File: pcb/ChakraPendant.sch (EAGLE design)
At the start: 12 parts

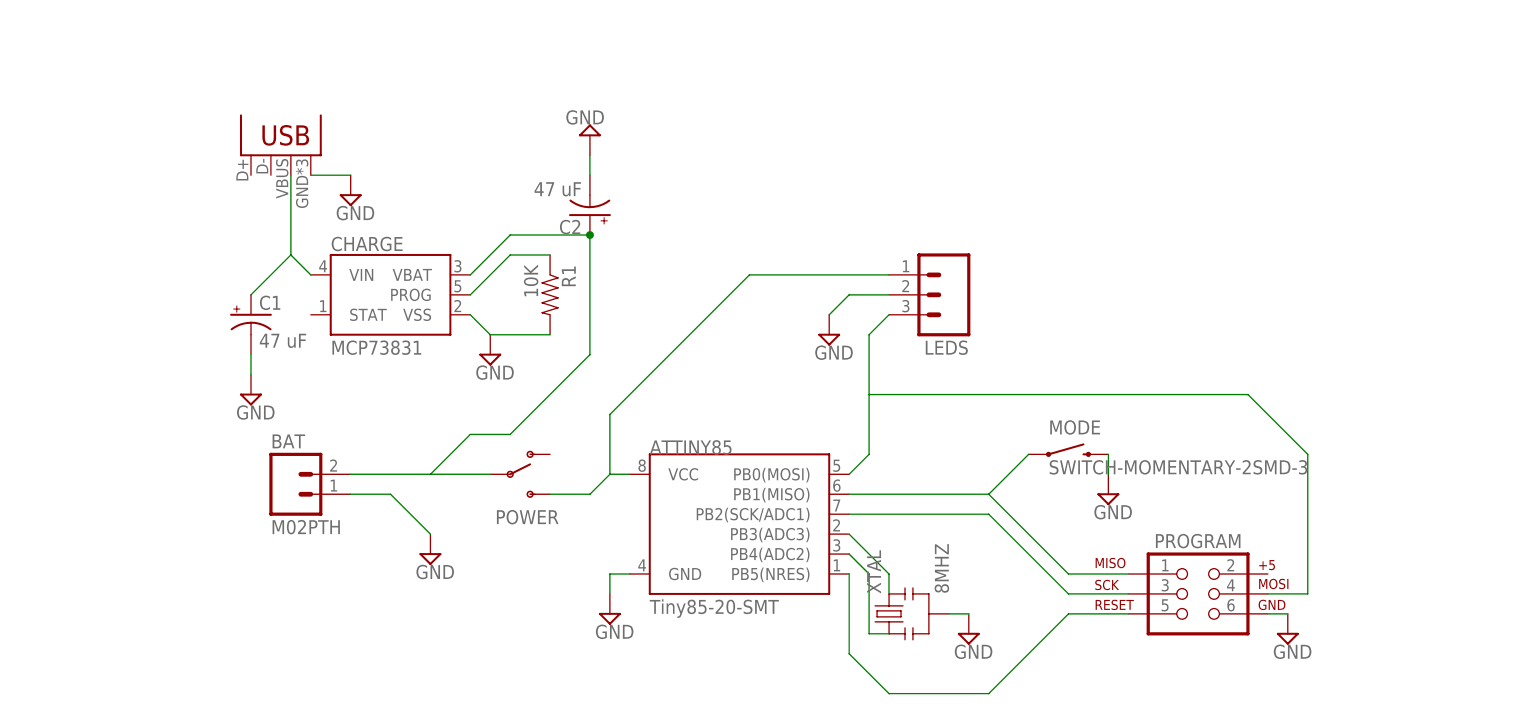
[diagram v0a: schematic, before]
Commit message: Remove power switches. Add Charge LEDs. Change ISP header to pogopin programmer.
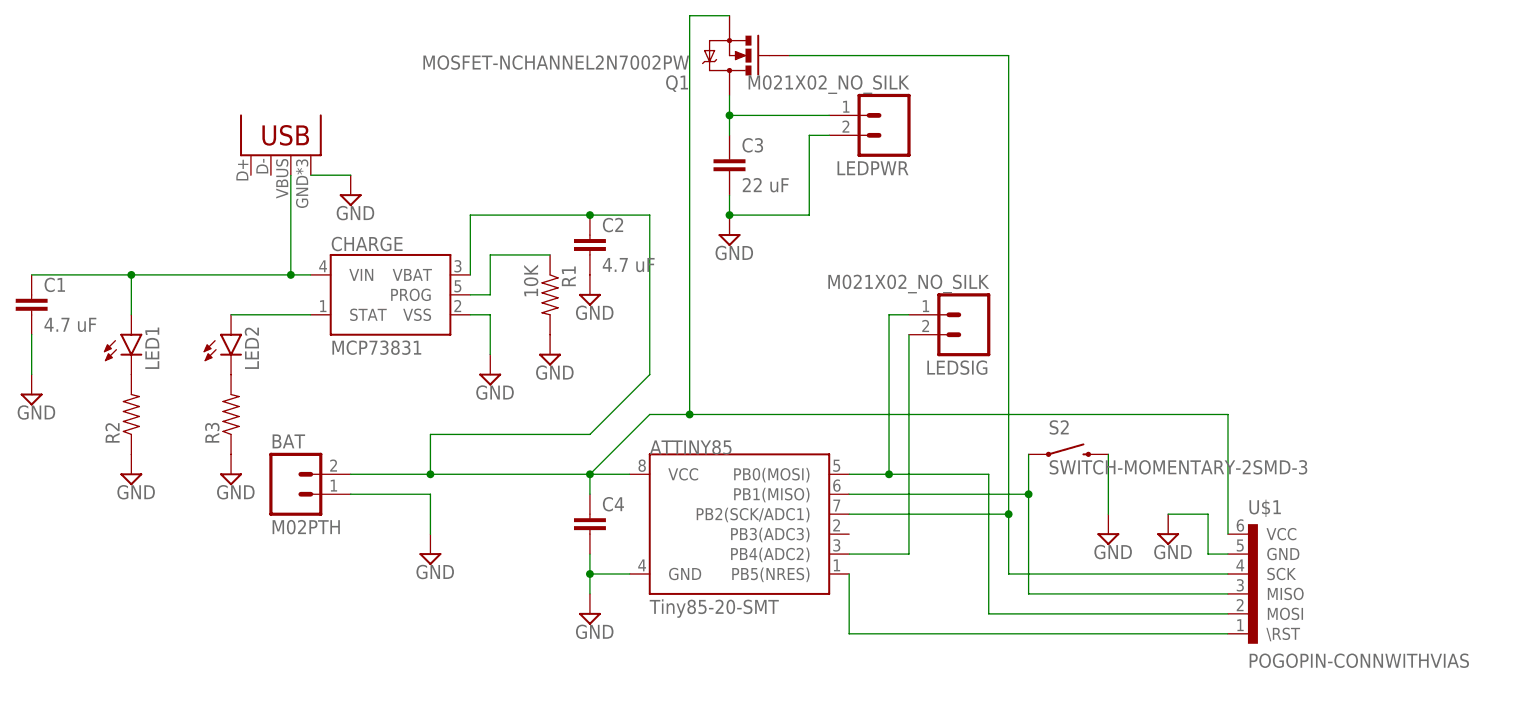
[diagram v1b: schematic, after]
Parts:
- removed LEDS: (no value), SparkFun-Connectors:M03PTH
- removed POWER: (no value), SparkFun-Electromechanical:SWITCH-SPDT-SMD-A
- removed PROGRAM: AVR_SPI_PRG_62X3_LOCK, SparkFun-Connectors:AVR_SPI_PRG_62X3_LOCK
- removed XTAL: 8MHZ, SparkFun-FreqCtrl:RESONATOR8MHZ
- added C3: 22 uF, SparkFun-Passives:CAP1206
- added C4: (no value), SparkFun-Passives:CAP0603-CAP
- added LED1, LED2: (no value), SparkFun-LED:LED0603
- added LEDPWR, LEDSIG: M021X02_NO_SILK, SparkFun-Connectors:M021X02_NO_SILK
- added Q1: MOSFET-NCHANNEL2N7002PW, SparkFun-DiscreteSemi:MOSFET-NCHANNEL2N7002PW
- added R2, R3: (no value), SparkFun-Passives:RESISTOR0603-RES
- added U$1: POGOPIN-CONNWITHVIAS, Protofusion:POGOPIN-CONNWITHVIAS
- C1, C2: value 47 uF -> 4.7 uF; device SparkFun-Capacitors:CAP_POL1206 -> SparkFun-Passives:CAP0603-CAP
- renumbered MODE to S2
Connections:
- removed net USBV+: C1.+, CHARGE.VIN, JP1.VBUS
- removed net VCC: ATTINY85.VCC, LEDS.1, POWER.S
- removed net XTAL1: ATTINY85.PB4(ADC2), XTAL.1
- removed net XTAL2: ATTINY85.PB3(ADC3), XTAL.3
- new net N$1: C3.1, LEDPWR.1, Q1.D
- new net N$2: C1.1, CHARGE.VIN, JP1.VBUS, LED1.A
- new net N$3: ATTINY85.PB4(ADC2), LEDSIG.2
- new net N$4: LED1.C, R2.2
- new net N$5: LED2.C, R3.2
- new net N$7: CHARGE.STAT, LED2.A
- net BATTV+: now also ATTINY85.VCC, C2.1, C4.1, Q1.S, U$1.VCC; no longer C2.+, POWER.P
- net GND: now also C1.2, C2.2, C3.2, C4.2, LEDPWR.2, R2.1, R3.1, U$1.GND; no longer C1.-, C2.-, LEDS.2, PROGRAM.6, XTAL.2
- net PB0-MOSI: now also LEDSIG.1, U$1.MOSI; no longer LEDS.3, PROGRAM.4
- net PB1-MISO: now also U$1.MISO; no longer PROGRAM.1
- net PB2-SCK: now also Q1.G, U$1.SCK; no longer PROGRAM.3
- net PB5-RESET: now also U$1.\RST; no longer PROGRAM.5

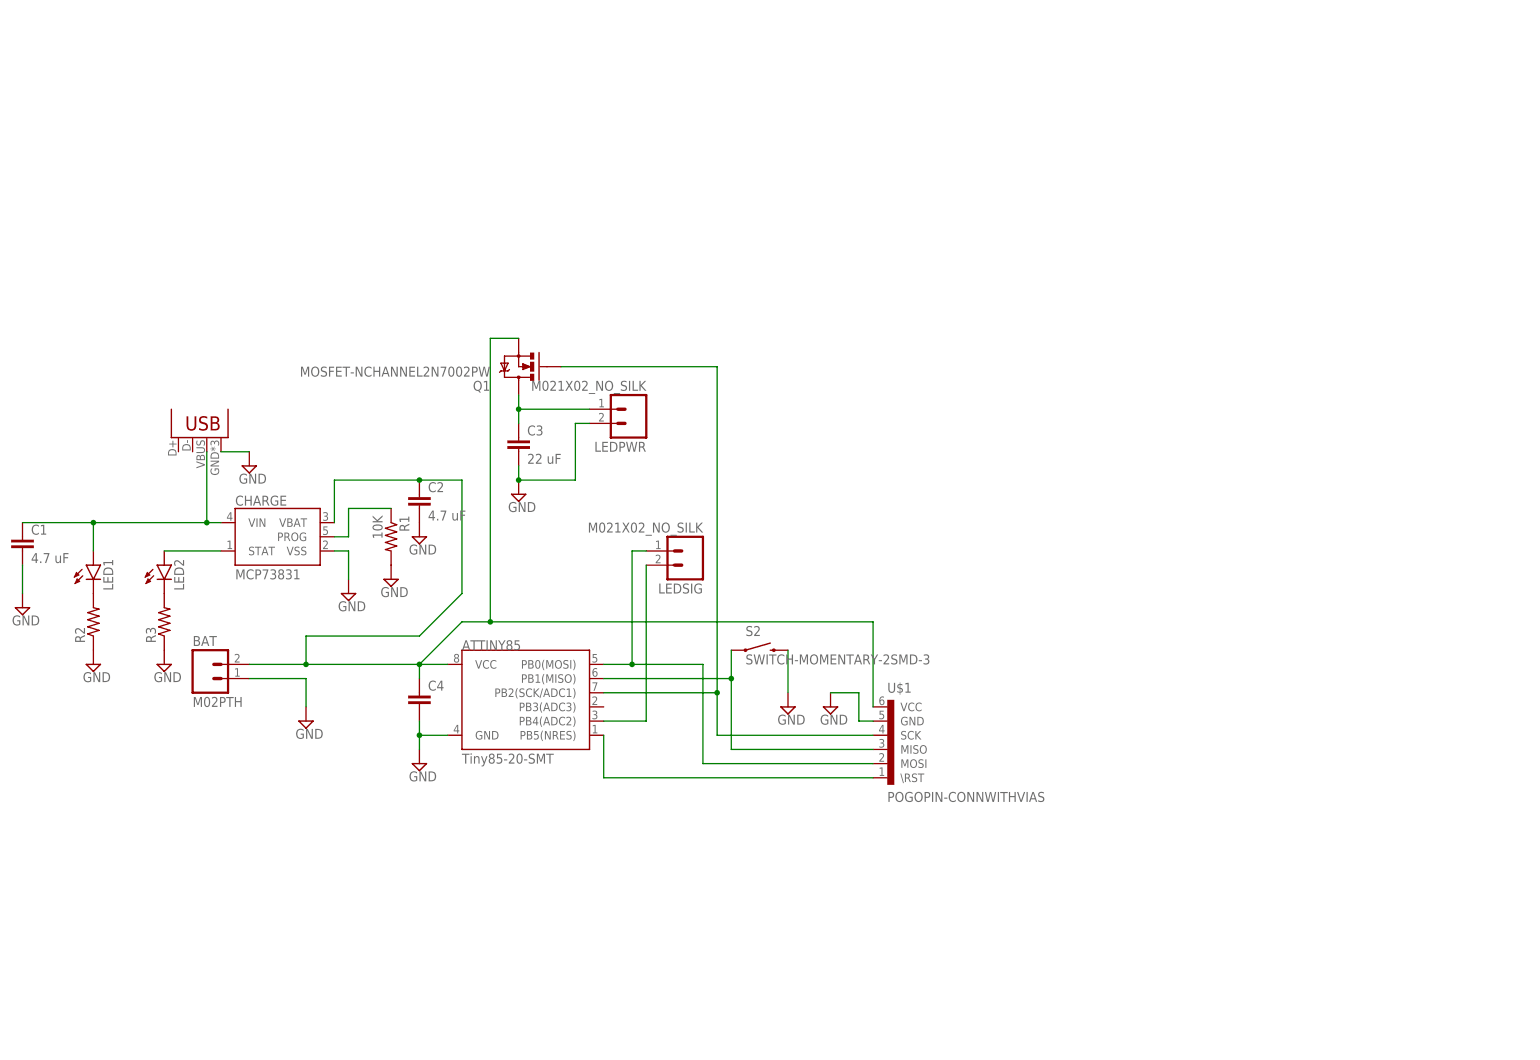
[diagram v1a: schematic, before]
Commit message: GREATLY cleaned up main board schematic. Piped charge STAT to chip
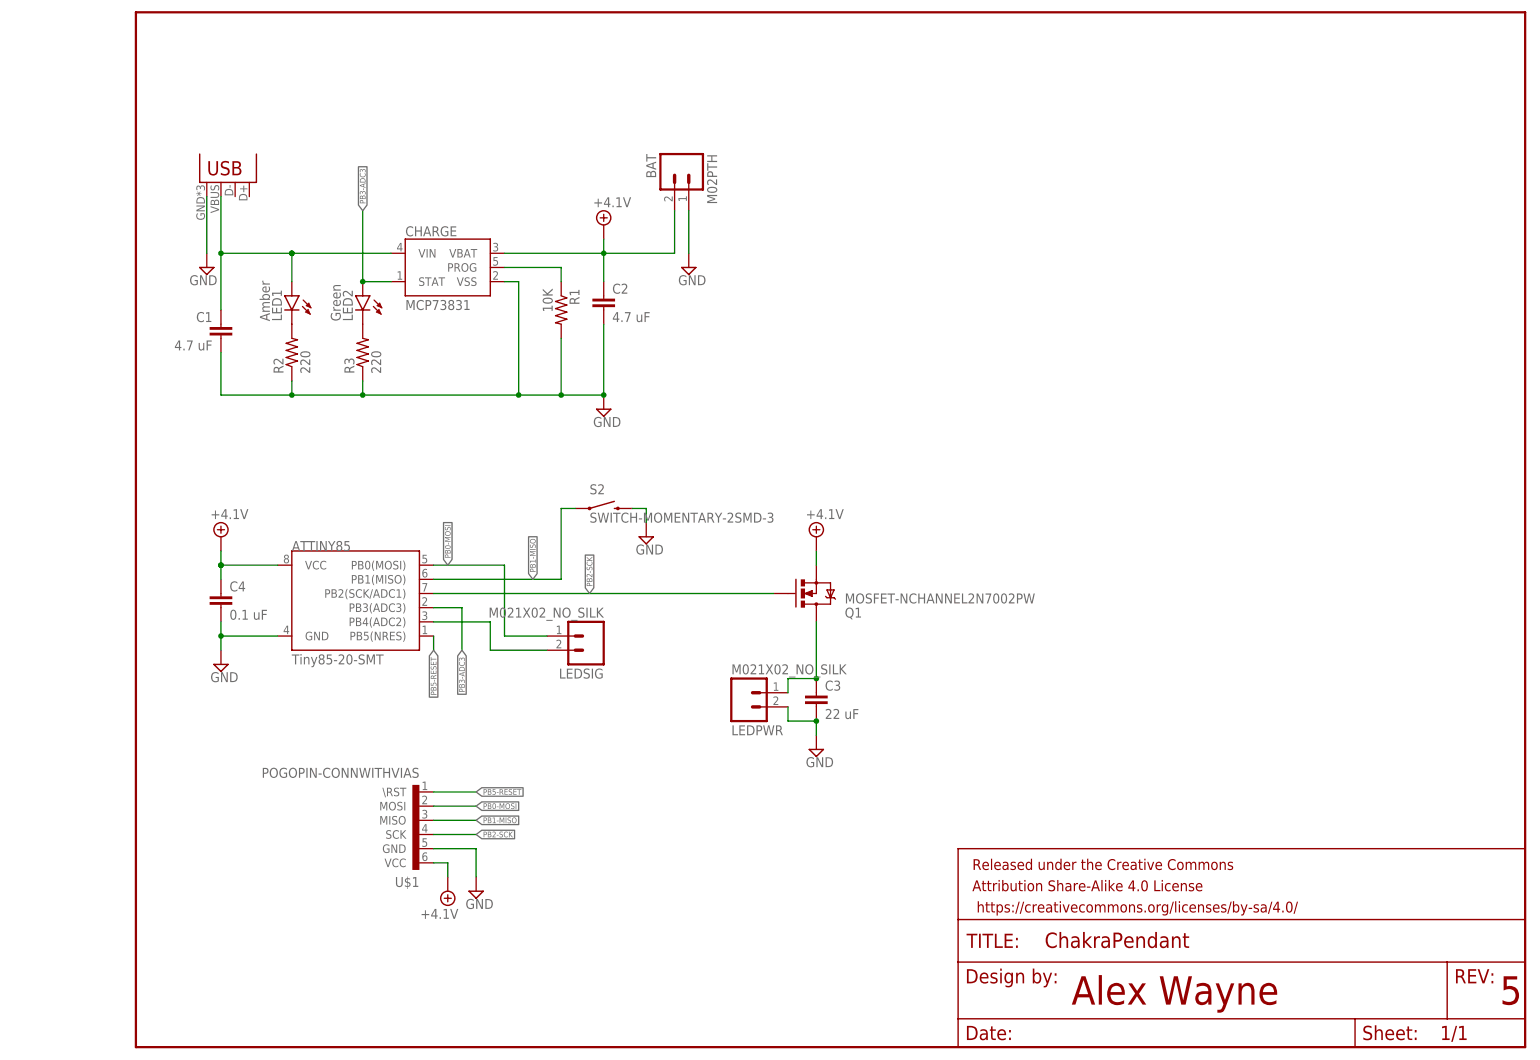
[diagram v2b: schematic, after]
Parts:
- added FRAME1: FRAME-LETTER, SparkFun-Aesthetics:FRAME-LETTER
- C4: value (none) -> 0.1 uF
- LED1: value (none) -> Amber
- LED2: value (none) -> Green
- R2, R3: value (none) -> 220
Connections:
- net BATTV+ renamed +4.1V
- net N$2 renamed USB5V
- removed net N$7: CHARGE.STAT, LED2.A
- new net PB3-ADC3: ATTINY85.PB3(ADC3), CHARGE.STAT, LED2.A
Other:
- note added: "5"
- note added: "Alex Wayne"
- moved on the sheet: ATTINY85, BAT, C1, C2, C3, C4, CHARGE, LED1, LED2, LEDPWR, LEDSIG, Q1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

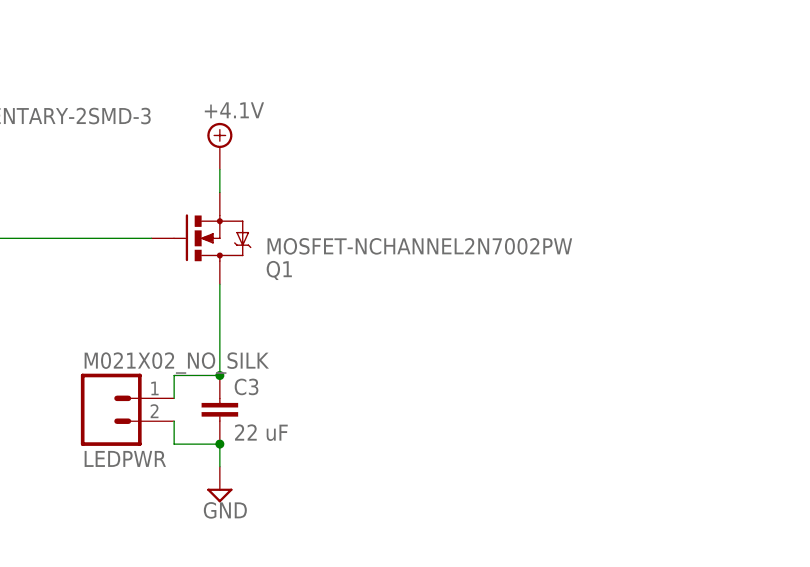
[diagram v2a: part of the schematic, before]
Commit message: Fix that MOSFET was wired backwards :(
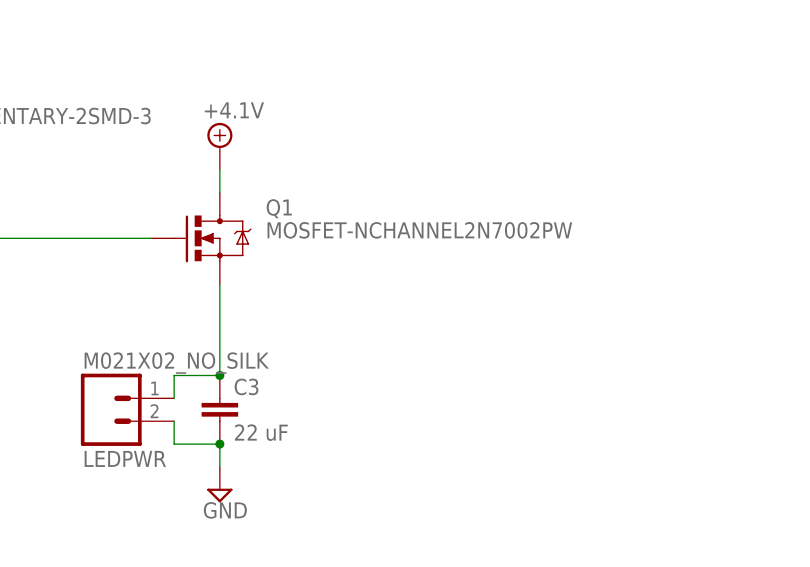
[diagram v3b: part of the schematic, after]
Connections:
- net +4.1V: now also Q1.D; no longer Q1.S
- net N$1: now also Q1.S; no longer Q1.D
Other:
- moved on the sheet: Q1
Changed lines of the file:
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@@
 <instance part="C2" gate="G$1" x="83.82" y="132.08"/>
 <instance part="C3" gate="G$1" x="121.92" y="60.96"/>
-<instance part="Q1" gate="G$1" x="121.92" y="81.28" rot="MR180"/>
+<instance part="Q1" gate="G$1" x="121.92" y="81.28"/>
 <instance part="U$1" gate="J" x="50.8" y="38.1" rot="R180"/>
 <instance part="S2" gate="G$1" x="83.82" y="96.52"/>
@@
 <net name="N$1" class="1">
 <segment>
-<pinref part="Q1" gate="G$1" pin="D"/>
 <pinref part="C3" gate="G$1" pin="1"/>
 <pinref part="LEDPWR" gate="G$1" pin="1"/>
-<wire x1="121.92" y1="66.04" x2="121.92" y2="76.2" width="0.1524" layer="91"/>
-<junction x="121.92" y="66.04"/>
 <wire x1="116.84" y1="63.5" x2="116.84" y2="66.04" width="0.1524" layer="91"/>
 <wire x1="116.84" y1="66.04" x2="121.92" y2="66.04" width="0.1524" layer="91"/>
+<pinref part="Q1" gate="G$1" pin="S"/>
+<wire x1="121.92" y1="76.2" x2="121.92" y2="66.04" width="0.1524" layer="91"/>
+<junction x="121.92" y="66.04"/>
 </segment>
 </net>
@@
 </segment>
 <segment>
-<pinref part="Q1" gate="G$1" pin="S"/>
-<wire x1="121.92" y1="86.36" x2="121.92" y2="88.9" width="0.1524" layer="91"/>
-<pinref part="SUPPLY11" gate="P" pin="+4.1V"/>
-</segment>
-<segment>
 <pinref part="BAT" gate="G$1" pin="2"/>
 <pinref part="CHARGE" gate="G$1" pin="VBAT"/>
@@
 <wire x1="15.24" y1="83.82" x2="15.24" y2="86.36" width="0.1524" layer="91"/>
 </segment>
-</net>
+<segment>
+<pinref part="Q1" gate="G$1" pin="D"/>
+<pinref part="SUPPLY11" gate="P" pin="+4.1V"/>
+<wire x1="121.92" y1="86.36" x2="121.92" y2="88.9" width="0.1524" layer="91"/>
+</segment>
+</net>
